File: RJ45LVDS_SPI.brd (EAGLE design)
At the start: 45.1 x 38.5 mm, 47 parts, among them J1 RJHSE-3381, U1 SN65MLVD206, U2 SN65MLVD206, U3 SN65MLVD206, U4 SN65MLVD206, U5 SN74LVC1T45DBVR, U6 SN74LVC1T45DBVR, U7 SN74LVC1T45DBVR, U8 SN74LVC1T45DBVR, U9 MIC39100-3.3WS

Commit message: layout tweaks
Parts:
- moved C16 10.3 mm to (49.0, 69.3), turned to 270 degrees
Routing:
- net +3V3: track 131.9 -> 156.0 mm
- net N$16: track 43.8 -> 31.5 mm
- net VCCIO: track 63.5 -> 73.5 mm
- net +5V: track 9.92 -> 18.9 mm

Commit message: Board tweaks and added gerbers
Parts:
- SJ10, SJ11, SJ12, SJ9: value (none) -> JUMPER; device jumper:SJ -> rcl-dhs:0603JMP
- moved R5 38.3 mm to (32.8, 32.7)
- moved C7 38.2 mm to (7.16, 8.51)
- moved C11 38.2 mm to (34.9, 32.7)
- moved C16 38.2 mm to (42.2, 31.7)
- moved J1 38.2 mm to (18.5, 28.4)
- moved JP1 38.2 mm to (34.4, 5.46)
- moved JP2 38.2 mm to (37.4, 36.2)
- moved SJ10 38.2 mm to (40.6, 27.9)
- moved SJ11 38.2 mm to (34.9, 10.1)
- moved SJ12 38.2 mm to (34.5, 20.8)
- moved SJ9 38.2 mm to (33.5, 13.8)
- moved U$2 38.2 mm to (40.1, 13.2)
- moved U1 38.2 mm to (28.7, 15.7)
- moved U2 38.2 mm to (21.1, 15.7)
- moved U3 38.2 mm to (5.84, 15.7)
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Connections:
- net +3V3: now also SJ12.P$2, SJ9.P$2; no longer SJ12.2, SJ9.2
- net +5V: now also SJ10.P$2; no longer SJ10.2
- net N$16: now also SJ10.P$1, SJ11.P$2; no longer SJ10.1, SJ11.2
- net N$17: now also SJ12.P$1; no longer SJ12.1
- net VCCIO: now also SJ11.P$1, SJ9.P$1; no longer SJ11.1, SJ9.1
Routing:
- net +3V3: track 156.0 -> 157.9 mm
- removed copper zone on layer 1, net GND
- removed copper zone on layer 16, net GND
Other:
- board size 45.1 x 38.5 mm -> 45.2 x 39.1 mm
- board text added: "DIRECTION SET JUMPERS <- OUTPUT"
- board text added: "INPUT ->"
- board text removed: "DIRECTION SET JUMPERS <- OUTPUT INPUT->"

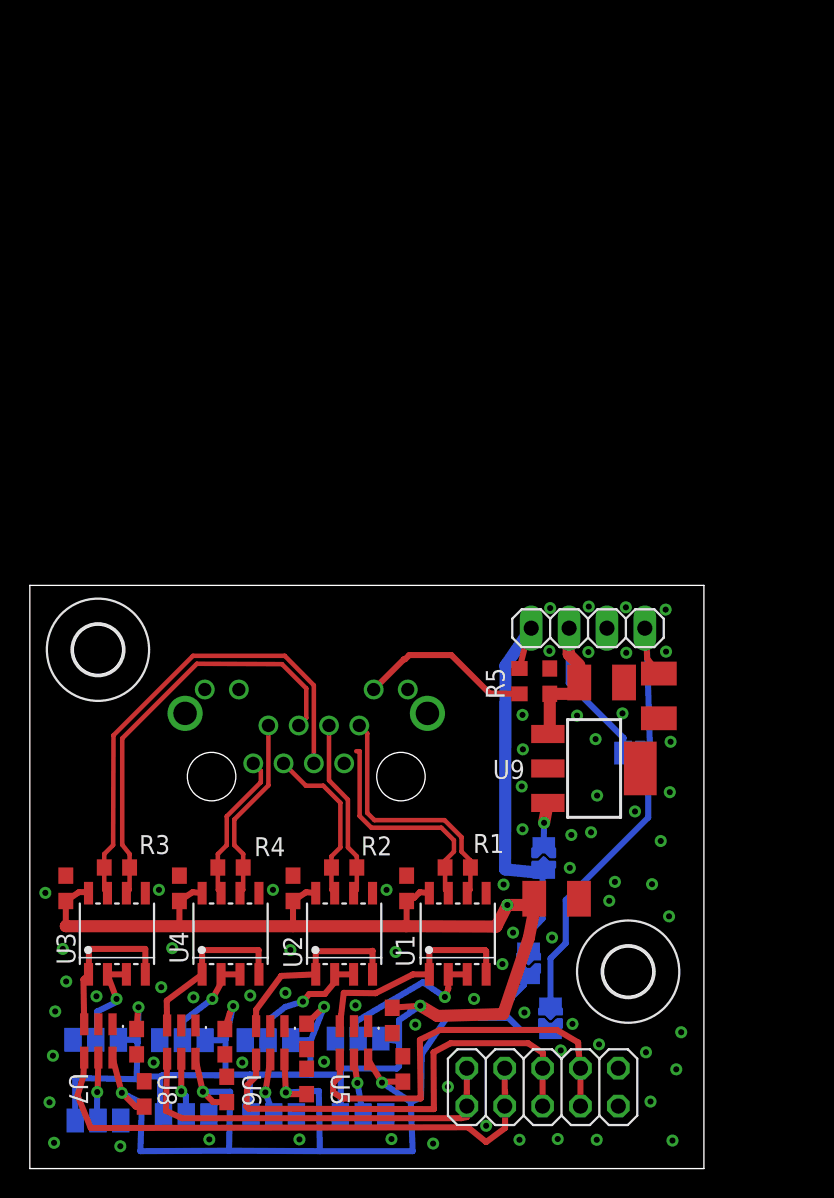
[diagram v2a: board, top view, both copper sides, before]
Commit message: Fixed problems with v1.0 board
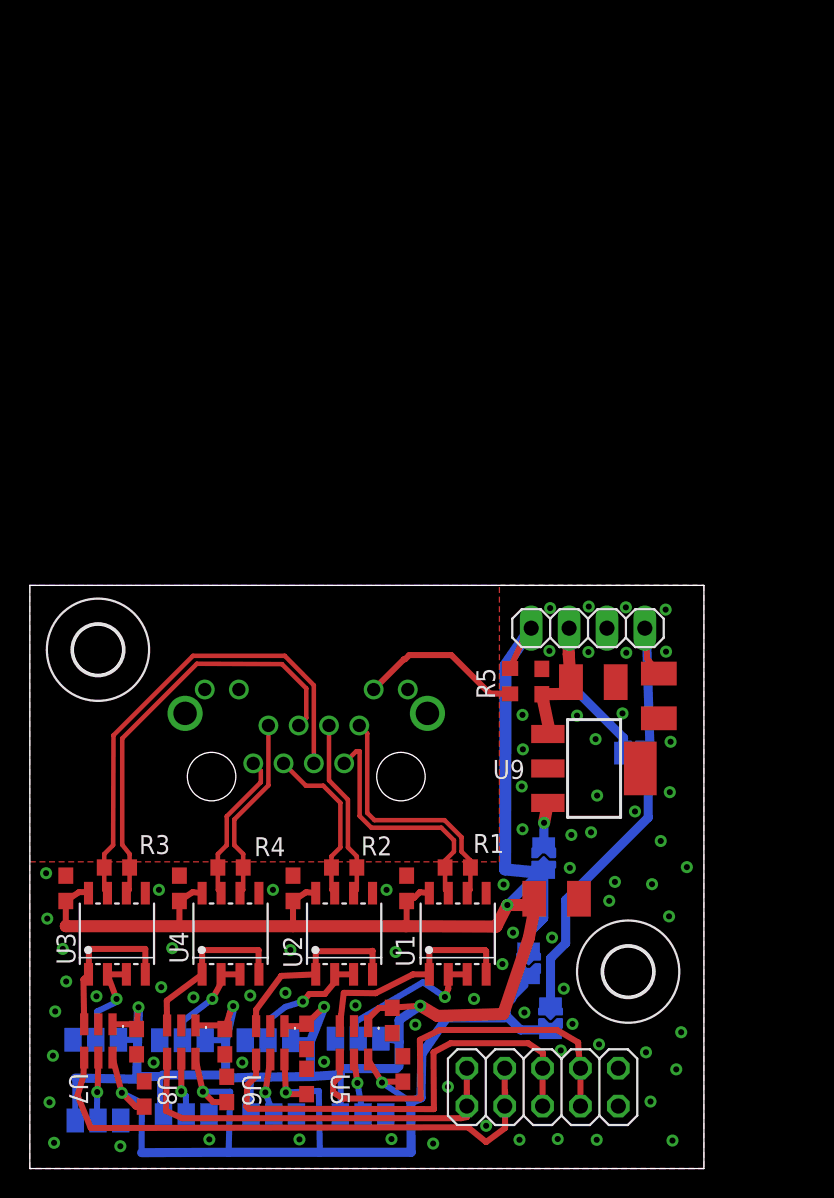
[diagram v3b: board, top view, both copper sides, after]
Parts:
- moved R5 0.63 mm to (32.2, 32.7)
- moved C10 0.56 mm to (37.8, 32.6)
- moved C11 0.53 mm to (34.3, 32.7)
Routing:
- net +3V3: track 157.9 -> 173.7 mm
- net IN1_N: track 15.5 -> 16.6 mm
- net N$19: track 11.8 -> 11.2 mm
- added copper zone on layer 1, net GND
- added copper zone on layer 16, net GND
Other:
- board text added: "LVDS on RJ45 to single-ended breakout NIST/DTCA/DHS v1.1 5/2017"
- board text added: "POWER"
- board text added: "UNREG to EXT V_LOGIC"
- board text removed: "LVDS on RJ45 to single-ended breakout NIST/DTCA/DHS v1.0 4/2017"
- board text removed: "UNREG-EXT"

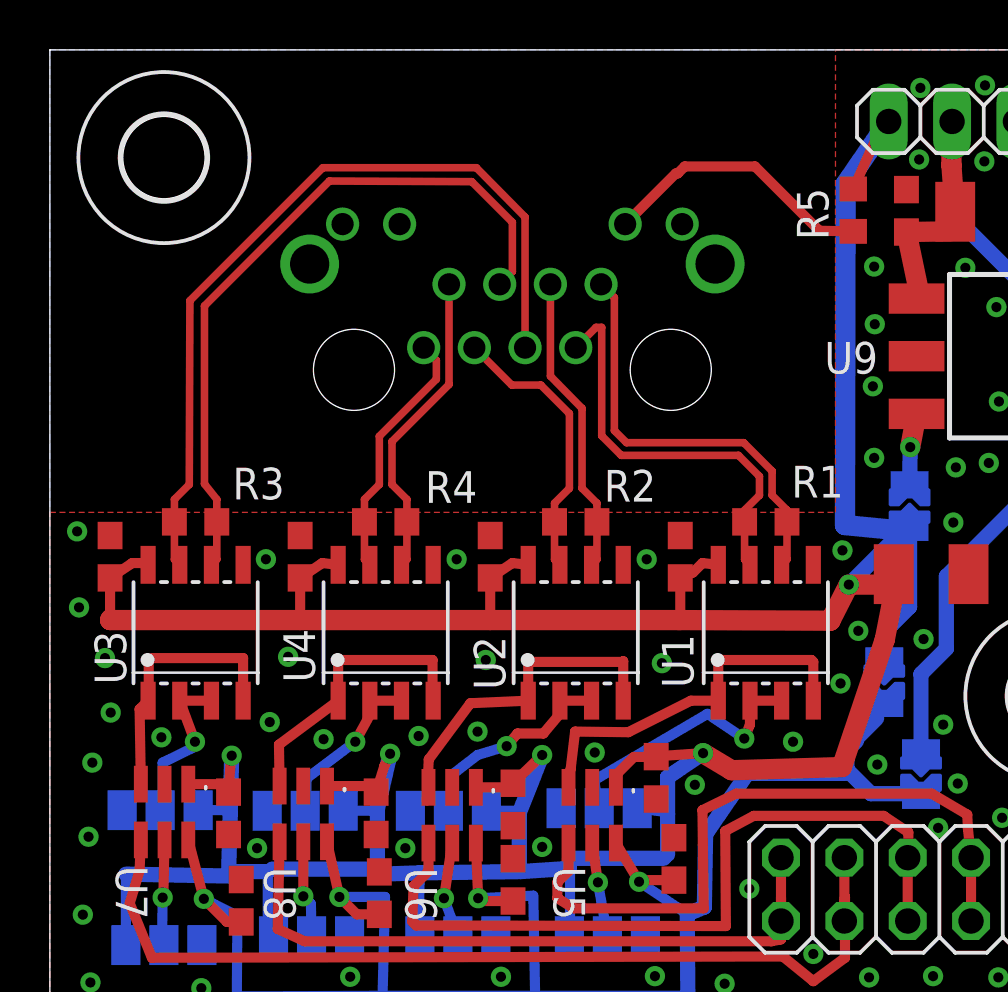
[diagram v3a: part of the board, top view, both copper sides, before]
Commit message: Changed RJ45 footprint
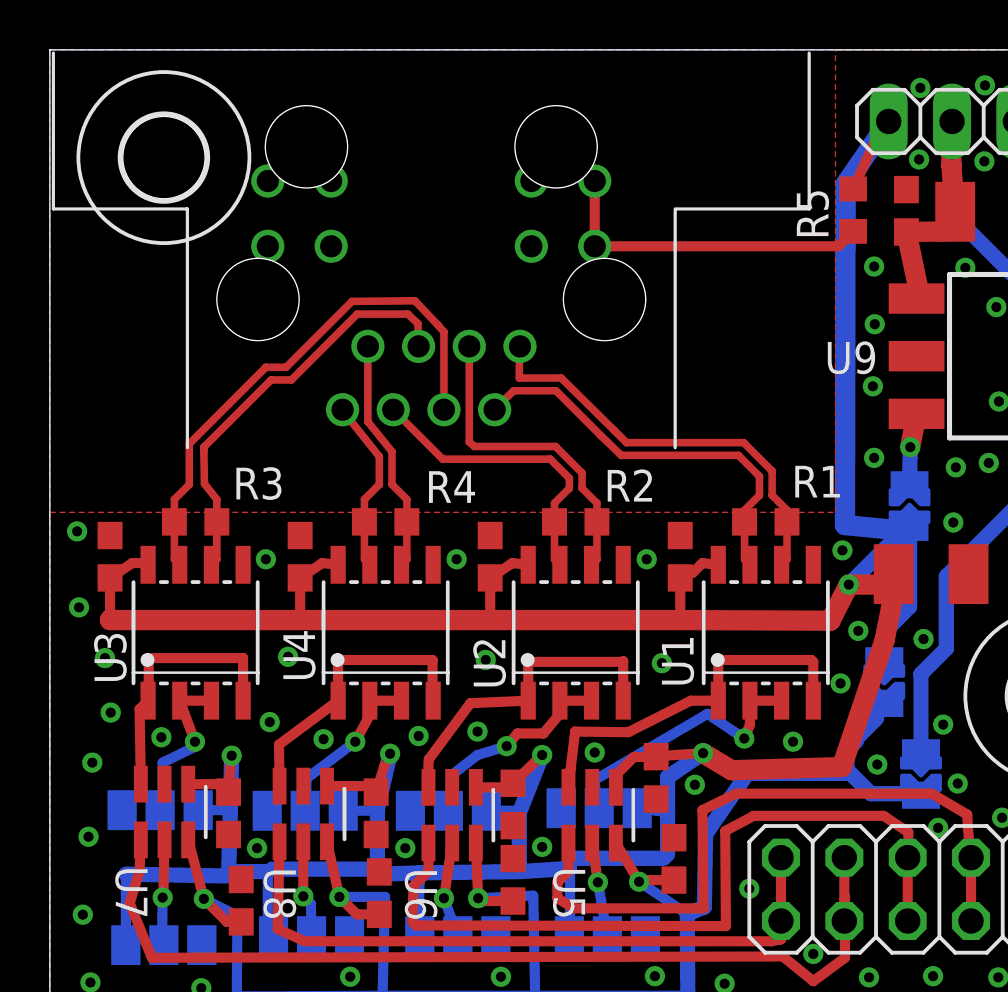
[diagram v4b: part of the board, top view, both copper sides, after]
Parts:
- removed J1: RJHSE-3381, artiq-ttl:RJHSE-338X
- added J2: MRJ, artiq-ttl:MRJ-MEGAMIX
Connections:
- net GND: now also J2.P$10A, J2.P$10B, J2.P$11A, J2.P$11B, J2.P$9A, J2.P$9B; no longer J1.P$11, J1.P$12, J1.P$13, J1.P$14, J1.P$9
- net IN1_N: now also J2.P$2; no longer J1.P$2
- net IN1_P: now also J2.P$1; no longer J1.P$1
- net IN2_N: now also J2.P$6; no longer J1.P$6
- net IN2_P: now also J2.P$3; no longer J1.P$3
- net IN3_N: now also J2.P$4; no longer J1.P$4
- net IN3_P: now also J2.P$5; no longer J1.P$5
- net IN4_N: now also J2.P$8; no longer J1.P$8
- net IN4_P: now also J2.P$7; no longer J1.P$7
- net N$19: now also J2.P$12A, J2.P$12B; no longer J1.P$10
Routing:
- net IN3_P: track 28.4 -> 16.8 mm
- net IN3_N: track 32.6 -> 21.4 mm
- net IN4_N: track 10.2 -> 7.06 mm
- net IN4_P: track 12.5 -> 9.43 mm
- net N$19: track 11.2 -> 13.2 mm
- net IN2_P: track 12.1 -> 12.9 mm
- net IN2_N: track 11.3 -> 12.0 mm
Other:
- board text added: "DIRECTION SET JUMPERS <- INTPUT"
- board text added: "LVDS on RJ45 to single-ended breakout NIST/DTCA/DHS v0.3 5/2017"
- board text added: "OUTPUT ->"
- board text removed: "DIRECTION SET JUMPERS <- OUTPUT"
- board text removed: "INPUT ->"
- board text removed: "LVDS on RJ45 to single-ended breakout NIST/DTCA/DHS v1.1 5/2017"

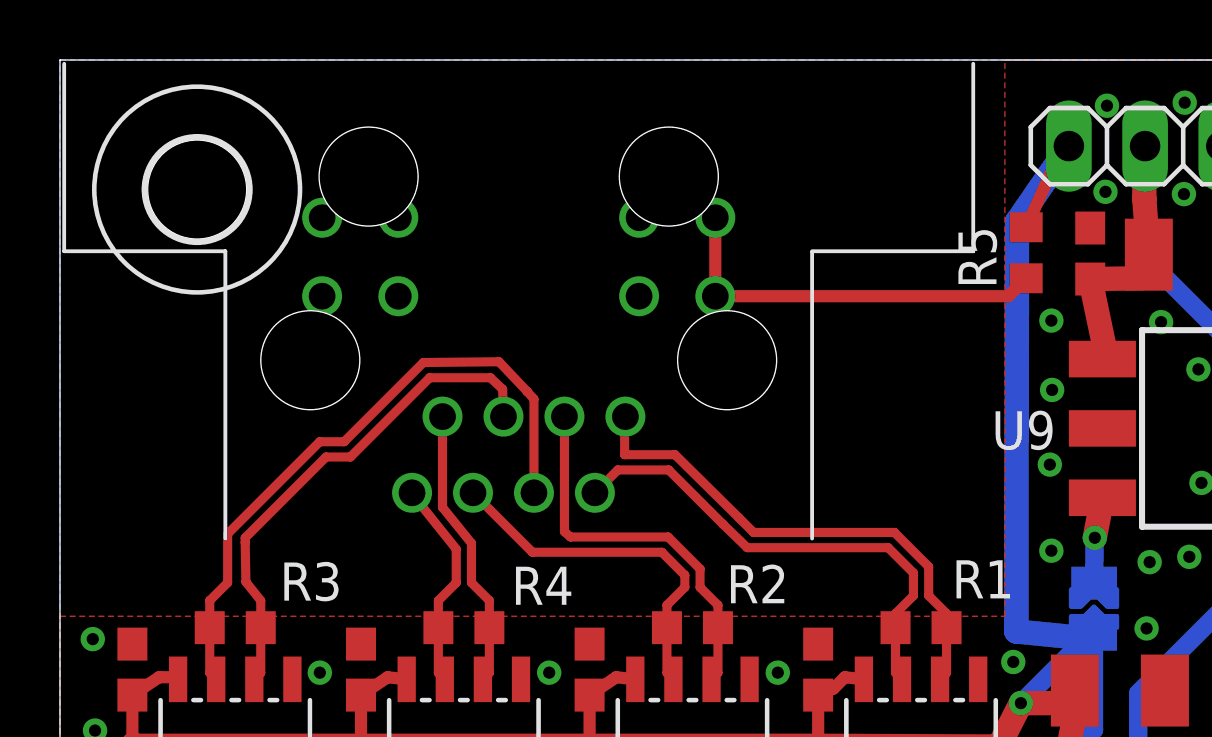
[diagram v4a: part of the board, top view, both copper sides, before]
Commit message: Fixed RJ45 footprint issue
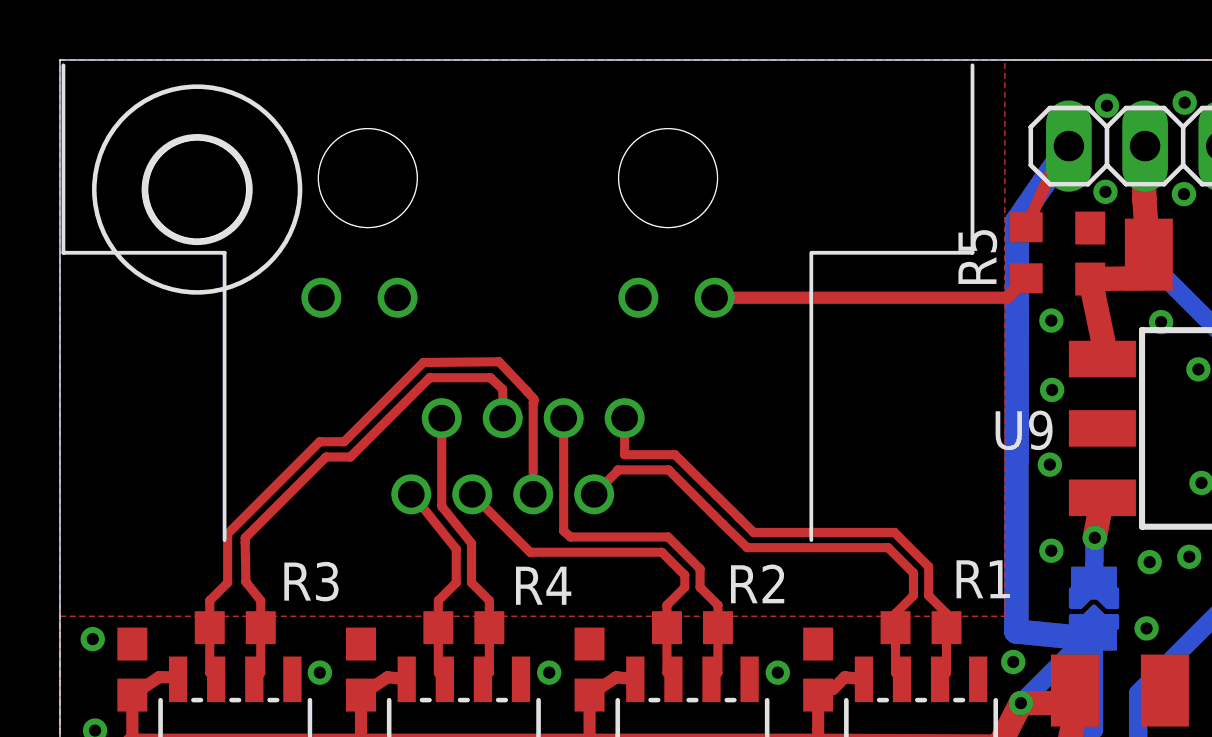
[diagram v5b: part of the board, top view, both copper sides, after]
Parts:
- removed J2: MRJ, artiq-ttl:MRJ-MEGAMIX
- added J1: MRJ, RJ45LVDS_SPI:MRJ-MEGAMIX
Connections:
- net GND: now also J1.P$10A, J1.P$11A, J1.P$9A; no longer J2.P$10A, J2.P$10B, J2.P$11A, J2.P$11B, J2.P$9A, J2.P$9B
- net IN1_N: now also J1.P$2; no longer J2.P$2
- net IN1_P: now also J1.P$1; no longer J2.P$1
- net IN2_N: now also J1.P$6; no longer J2.P$6
- net IN2_P: now also J1.P$3; no longer J2.P$3
- net IN3_N: now also J1.P$4; no longer J2.P$4
- net IN3_P: now also J1.P$5; no longer J2.P$5
- net IN4_N: now also J1.P$8; no longer J2.P$8
- net IN4_P: now also J1.P$7; no longer J2.P$7
- net N$19: now also J1.P$12A; no longer J2.P$12A, J2.P$12B
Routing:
- net N$19: track 13.2 -> 10.7 mm

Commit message: v0.4 changes
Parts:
- added C17: .1u, rcl-dhs:C0603
- added JP3: (no value), pinhead:1X02
- added U$3: (no value), holes:3,3
- added U10: 74AHC1GU04DCK, 74xx-little-us:SC70-5
- JP1: device pinhead:2X05 -> pinhead:2X06
- SJ1, SJ2, SJ3, SJ4, SJ5, SJ6, SJ7, SJ8: device jumper:SJ_2 -> RJ45LVDS_SPI:SJ_2
- moved U9 2.95 mm to (39.0, 24.1)
- moved C16 2.39 mm to (43.0, 29.5)
- moved C10 2.09 mm to (37.9, 30.5)
- moved C11 1.98 mm to (34.4, 30.7)
- moved JP1 1.24 mm to (35.6, 5.44)
- moved R5 1.09 mm to (32.2, 31.6), turned to 0 degrees
- moved JP2 0.18 mm to (37.5, 36.1)
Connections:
- new net A: JP3.1, U10.2
- new net NOT_A: JP3.2, U10.4
- net +3V3: now also JP1.1, JP1.2
- net GND: now also C17.2, JP1.3, JP1.4, U10.3; no longer JP1.1, JP1.2
- net N$13: now also JP1.5, JP1.6; no longer JP1.3, JP1.4
- net N$14: now also JP1.7, JP1.8; no longer JP1.5, JP1.6
- net N$15: now also JP1.10, JP1.9; no longer JP1.7, JP1.8
- net N$8: now also JP1.11, JP1.12; no longer JP1.10, JP1.9
- net VCCIO: now also C17.1, U10.5
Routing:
- net VCCIO: track 73.5 -> 98.0 mm, vias 4 -> 5
- net GND: track 0.00 -> 21.3 mm, vias 77 -> 81
- net +3V3: track 173.7 -> 191.2 mm
- net A: track 0.00 -> 4.62 mm
- net NOT_A: track 0.00 -> 3.53 mm
- net +5V: track 18.9 -> 21.9 mm
- net N$16: track 31.3 -> 33.4 mm
- net N$15: track 39.4 -> 37.4 mm
- net N$8: track 28.0 -> 26.9 mm
- net N$17: track 2.70 -> 3.61 mm
- net IN4_N: track 6.79 -> 7.63 mm
- net N$19: track 10.7 -> 9.86 mm
- net N$21: track 0.00 -> 0.69 mm
- net N$18: track 0.00 -> 0.69 mm
- net N$23: track 0.00 -> 0.58 mm
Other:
- board text added: "3.3V"
- board text added: "INV IN"
- board text added: "INV OUT"
- board text added: "LVDS on RJ45 to single-ended breakout NIST/DTCA/DHS v0.4 6/2017"
- board text removed: "LVDS on RJ45 to single-ended breakout NIST/DTCA/DHS v0.3 5/2017"
